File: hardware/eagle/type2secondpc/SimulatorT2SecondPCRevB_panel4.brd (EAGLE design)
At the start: 99.1 x 99.1 mm, 28 parts

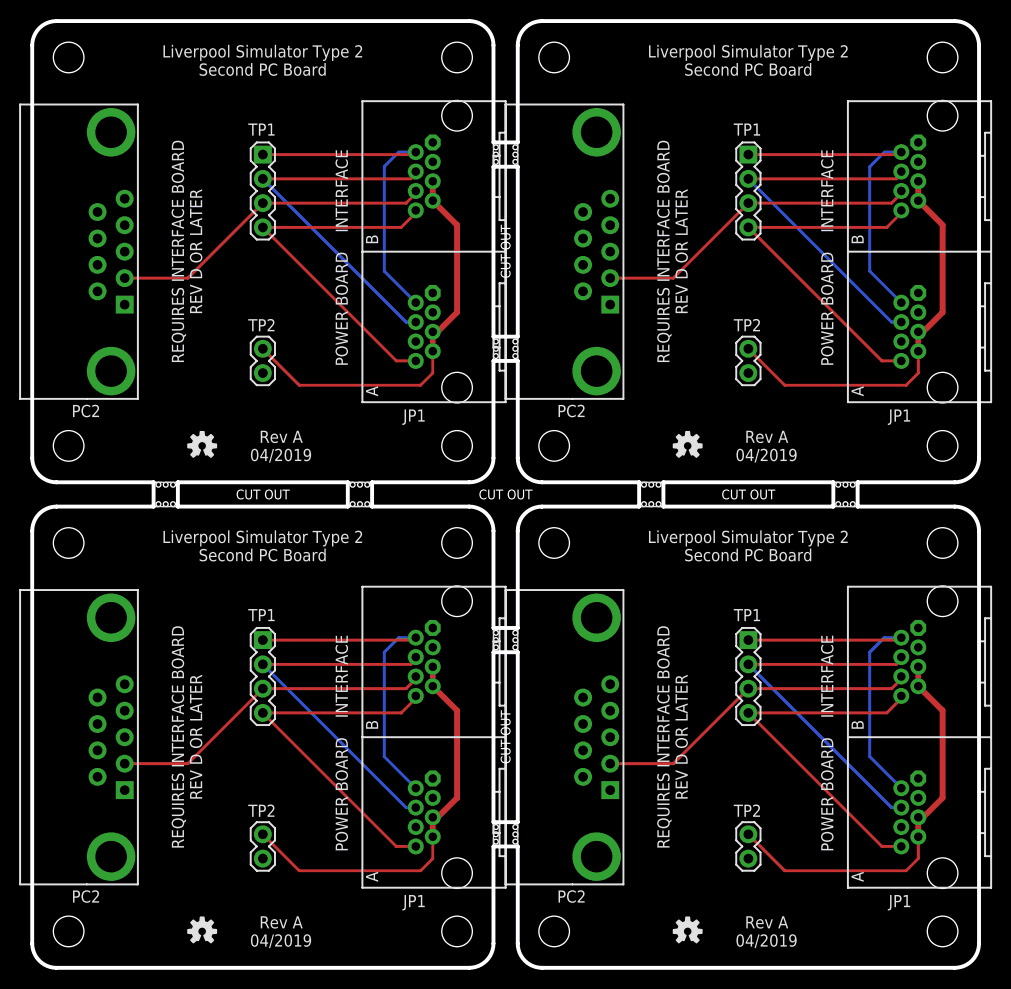
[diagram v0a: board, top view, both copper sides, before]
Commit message: Enhanced surge protection
Power Rev D, 2nd PC Rev B boards with improved surge protection,
Gerbers, Cost Estimation tool, New enclosure drilling templates.
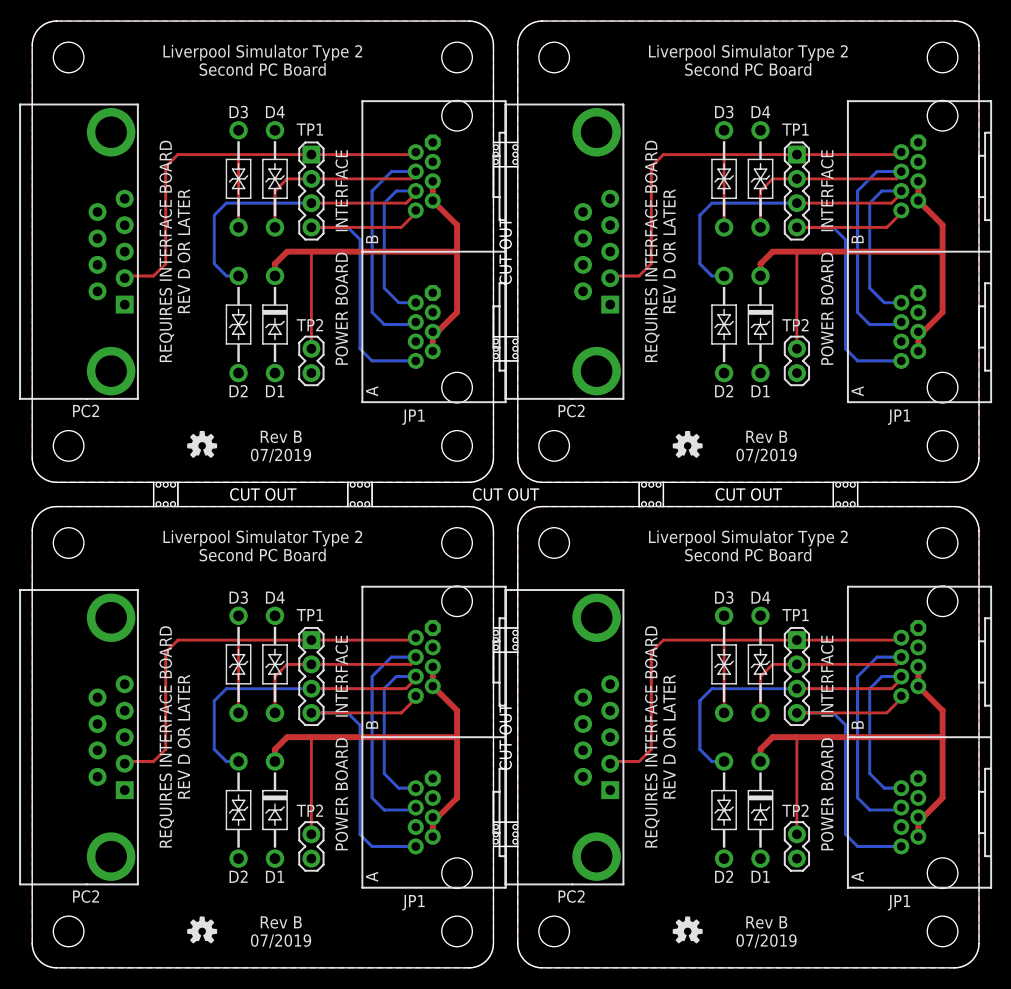
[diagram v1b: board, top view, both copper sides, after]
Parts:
- removed E$2, E$3, E$4, E$5, E$6, E$7, E$8: (no value), AIC_Custom:STAMP_HOLES
- added D1, D1_1, D1_2, D1_3: SA12A, AIC_Custom:DO41_TVS_UNI
- added D2, D2_1, D2_2, D2_3, D3, D3_1, D3_2, D3_3, D4, D4_1, D4_2, D4_3: SA15CA, AIC_Custom:DO41_TVS_BI
- E$1: device AIC_Custom:STAMP_HOLES -> AIC_Custom:OUTLINE_PANEL_4
- moved E$1 51.5 mm to (0.00, 0.00)
- moved TP1 5.08 mm to (29.2, 34.3)
- moved TP1_2 5.08 mm to (29.2, 85.1)
- moved TP2 5.08 mm to (29.2, 14.0)
- moved TP2_2 5.08 mm to (29.2, 64.8)
- moved TP1_1 5.08 mm to (80.0, 34.3)
- moved TP1_3 5.08 mm to (80.0, 85.1)
- moved TP2_1 5.08 mm to (80.0, 14.0)
- moved TP2_3 5.08 mm to (80.0, 64.8)
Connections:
- net GND: now also D1.ANODE, D2.A, D3.A, D4.A
- net GND1: now also D1_1.ANODE, D2_1.A, D3_1.A, D4_1.A
- net GND2: now also D1_2.ANODE, D2_2.A, D3_2.A, D4_2.A
- net GND3: now also D1_3.ANODE, D2_3.A, D3_3.A, D4_3.A
- net RXD: now also D4.C
- net RXD1: now also D4_1.C
- net RXD2: now also D4_2.C
- net RXD3: now also D4_3.C
- net TX2: now also D2.C, JP1.A2; no longer PC2.2
- net TX21: now also D2_1.C, JP1_1.A2; no longer PC2_1.2
- net TX22: now also D2_2.C, JP1_2.A2; no longer PC2_2.2
- net TX23: now also D2_3.C, JP1_3.A2; no longer PC2_3.2
- net TXD: now also D3.C, PC2.2; no longer JP1.A2
- net TXD1: now also D3_1.C, PC2_1.2; no longer JP1_1.A2
- net TXD2: now also D3_2.C, PC2_2.2; no longer JP1_2.A2
- net TXD3: now also D3_3.C, PC2_3.2; no longer JP1_3.A2
- net VIN2: now also D1.CATHODE
- net VIN21: now also D1_1.CATHODE
- net VIN22: now also D1_2.CATHODE
- net VIN23: now also D1_3.CATHODE
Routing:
- net TXD2: track 35.6 -> 49.5 mm
- net TXD3: track 35.6 -> 49.5 mm
- net TXD: track 35.6 -> 49.5 mm
- net TXD1: track 35.6 -> 49.5 mm
- net TX21: track 34.4 -> 47.1 mm
- net TX23: track 34.4 -> 47.1 mm
- net TX2: track 34.4 -> 47.1 mm
- net TX22: track 34.4 -> 47.1 mm
- net VIN23: track 42.4 -> 51.2 mm
- net VIN22: track 42.4 -> 51.2 mm
- net VIN21: track 42.4 -> 51.2 mm
- net VIN2: track 42.4 -> 51.2 mm
- net RXD3: track 38.7 -> 42.8 mm
- net RXD1: track 38.7 -> 42.8 mm
- net RXD: track 38.7 -> 42.8 mm
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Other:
- board text added: "D1"
- board text added: "D2"
- board text added: "D3"
- board text added: "D4"
- board text added: "Rev B 07/2019"
- board text removed: "CUT OUT"
- board text removed: "Rev A 04/2019"
